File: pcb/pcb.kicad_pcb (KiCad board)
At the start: 2 copper layers, 4 parts, among them U1 MCP2542FDxMF, U2 STM32G0B1KBUx, U3 MCP1792x-3302xCB

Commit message: unrouted nets 0
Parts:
- added C1: 2.2u, Capacitor_SMD:C_0603_1608Metric, F.Cu at (206.8, 53.3)
- added C10: 100n, Capacitor_SMD:C_0402_1005Metric, F.Cu at (185.4, 61.8)
- added C11: 100n, Capacitor_SMD:C_0402_1005Metric, F.Cu at (189.3, 54.7)
- added C12: 100n, Capacitor_SMD:C_0402_1005Metric, F.Cu at (190.6, 53.3)
- added C13: 4.7u, Capacitor_SMD:C_0603_1608Metric, F.Cu at (188.9, 53.3)
- added C2: 2.2u, Capacitor_SMD:C_0603_1608Metric, F.Cu at (212.1, 54.0)
- added C3: 100n, Capacitor_SMD:C_0402_1005Metric, F.Cu at (212.2, 64.8)
- added C4: 1u, Capacitor_SMD:C_0603_1608Metric, F.Cu at (210.8, 64.3)
- added C5: 1u, Capacitor_SMD:C_0402_1005Metric, F.Cu at (206.9, 62.6)
- added C6: 1u, Capacitor_SMD:C_0402_1005Metric, F.Cu at (206.9, 60.5)
- added C7: 100n, Capacitor_SMD:C_0402_1005Metric, F.Cu at (184.7, 53.8)
- added C8: 1u, Capacitor_SMD:C_0603_1608Metric, F.Cu at (186.2, 54.2)
- added C9: 100n, Capacitor_SMD:C_0402_1005Metric, F.Cu at (189.4, 64.1)
- added J1: Conn_01x04_MountingPin, goatworks-footprint-library:CONN04_5055670471_MOL, F.Cu at (215.9, 57.5)
- added J2: Conn_01x04_MountingPin, goatworks-footprint-library:CONN04_5055670471_MOL, F.Cu at (181.2, 60.9)
- added J4: Conn_ARM_SWD_TagConnect_TC2030-NL, Connector:Tag-Connect_TC2030-IDC-NL_2x03_P1.27mm_Vertical, F.Cu at (201.7, 54.2)
- added JP1: SolderJumper_2_Open, Jumper:SolderJumper-2_P1.3mm_Open_RoundedPad1.0x1.5mm, F.Cu at (206.9, 65.1)
- added LS1: Speaker_Crystal, goatworks-footprint-library:PKMCS0909E4000-R1, F.Cu at (201.0, 61.5)
- added M2: ~, goatworks-footprint-library:MP34DT05-A, F.Cu at (214.9, 64.2)
- moved U3 106.3 mm to (209.4, 54.6), turned to -45 degrees
- moved U2 92.8 mm to (192.9, 56.1), turned to -45 degrees
- moved U1 86.9 mm to (186.8, 64.1), turned to 180 degrees
- moved M1 77.2 mm to (182.2, 54.2), turned to 90 degrees
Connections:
- M1 pad 2: unconnected-(M1-LR-Pad2) -> GND
- M1 pad 3: unconnected-(M1-CLK-Pad3) -> /SCL
- M1 pad 4: unconnected-(M1-DOUT-Pad4) -> /SDA
- U1 pad 1: unconnected-(U1-TXD-Pad1) -> /CAN_TX
- U1 pad 2: Net-(U1-VSS-Pad2) -> GND
- U1 pad 3: unconnected-(U1-VDD-Pad3) -> +5V
- U1 pad 4: unconnected-(U1-RXD-Pad4) -> /CAN_RX
- U1 pad 5: unconnected-(U1-VIO-Pad5) -> +3V3
- U1 pad 8: unconnected-(U1-STBY-Pad8) -> /STBY
- U1 pad 9: Net-(U1-VSS-Pad2) -> GND
- U2 pad 11: unconnected-(U2-PA4-Pad11) -> /SPEAKER
- U2 pad 15: unconnected-(U2-PB0-Pad15) -> /CAN_RX
- U2 pad 16: unconnected-(U2-PB1-Pad16) -> /CAN_TX
- U2 pad 24: unconnected-(U2-PA13-Pad24) -> /SWDIO
- U2 pad 25: unconnected-(U2-PA14-Pad25) -> /SWCLK
- U2 pad 27: unconnected-(U2-PB3-Pad27) -> /SCL
- U2 pad 28: unconnected-(U2-PB4-Pad28) -> /SDA
- U2 pad 33: Net-(U2-VSS-Pad33) -> GND
- U2 pad 4: unconnected-(U2-VDD-Pad4) -> +3V3
- U2 pad 5: Net-(U2-VSS-Pad33) -> GND
- U2 pad 6: unconnected-(U2-PF2-Pad6) -> /RESET
- U3 pad 1: unconnected-(U3-GND-Pad1) -> GND
- U3 pad 2: unconnected-(U3-VO-Pad2) -> +3V3
- U3 pad 3: unconnected-(U3-VI-Pad3) -> +5V
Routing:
- net +3V3: track 0.00 -> 77.9 mm, vias 0 -> 4
- net /SCL: track 0.00 -> 57.2 mm, vias 0 -> 3
- net /SDA: track 0.00 -> 49.8 mm, vias 0 -> 3
- net +5V: track 0.00 -> 43.4 mm, vias 0 -> 3
- net /CANL: track 0.00 -> 42.2 mm, vias 0 -> 2
- net /CANH: track 0.00 -> 41.8 mm, vias 0 -> 2
- net /RESET: track 0.00 -> 14.6 mm, vias 0 -> 2
- net /SPEAKER: track 0.00 -> 9.76 mm, vias 0 -> 2
- net /CAN_TX: track 0.00 -> 9.14 mm
- net /CAN_RX: track 0.00 -> 7.95 mm
- net /SWDIO: track 0.00 -> 7.83 mm
- net Net-(JP1-A): track 0.00 -> 6.60 mm
- net /SWCLK: track 0.00 -> 6.53 mm
- net GND: track 0.00 -> 4.26 mm, vias 0 -> 25
- added copper zone on B.Cu, net GND
- added copper zone on F.Cu, net GND
- added copper zone on In1.Cu, net GND
- added copper zone on In2.Cu, net GND
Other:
- board outline added: 40 x 15 mm
- copper layers 2 -> 4

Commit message: drc
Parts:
- moved JP1 0.70 mm to (207.6, 65.1)
- moved LS1 0.30 mm to (201.3, 61.5)
- moved C11 0.10 mm to (189.2, 54.7)
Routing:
- net /SCL: track 57.2 -> 53.4 mm
- net GND: track 4.26 -> 7.14 mm, vias 25 -> 28
- net Net-(JP1-A): track 6.60 -> 7.30 mm
- net /CANL: track 42.2 -> 41.5 mm

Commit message: more vias
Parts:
- moved J4 0.63 mm to (201.5, 54.8)
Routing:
- net +3V3: track 78.1 -> 73.3 mm, vias 4 -> 5
- net GND: track 7.14 -> 7.19 mm, vias 28 -> 35

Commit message: improve routing
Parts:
- removed C5, C6: 1u, Capacitor_SMD:C_0402_1005Metric
- removed JP1: SolderJumper_2_Open, Jumper:SolderJumper-2_P1.3mm_Open_RoundedPad1.0x1.5mm
- added C14: 4.7u, Capacitor_SMD:C_0603_1608Metric, F.Cu at (194.6, 61.6)
- moved C10 0.80 mm to (186.2, 61.8)
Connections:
- LS1 pad 1: Net-(JP1-A) -> GND
- LS1 pad 2: /SPEAKER -> Net-(C14-Pad2)
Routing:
- net +3V3: track 73.3 -> 64.3 mm
- net Net-(JP1-A): track 7.30 -> 0.00 mm
- net /SCL: track 53.4 -> 49.9 mm
- net /SPEAKER: track 9.76 -> 7.52 mm
- net GND: track 7.19 -> 8.87 mm, vias 35 -> 41
- net Net-(C14-Pad2): track 0.00 -> 1.59 mm
- net /SDA: track 49.7 -> 50.9 mm
- net /SWCLK: track 6.58 -> 7.62 mm
- net /RESET: track 15.2 -> 16.0 mm
- net /CANH: track 41.8 -> 42.4 mm
- net +5V: track 43.4 -> 44.0 mm

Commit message: re route!!!
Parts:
- added C15: 100n, Capacitor_SMD:C_0402_1005Metric, F.Cu at (176.3, 52.4)
- added C16: 100n, Capacitor_SMD:C_0402_1005Metric, F.Cu at (226.2, 66.5)
- added D1: CAN_TVS, Package_TO_SOT_SMD:SOT-23-3, F.Cu at (188.0, 64.5)
- added M3: ~, goatworks-footprint-library:T3902, F.Cu at (173.5, 53.1)
- added M4: ~, goatworks-footprint-library:T3902, F.Cu at (223.0, 65.2)
- moved C2 21.1 mm to (191.1, 56.0), turned to 0 degrees
- moved U3 19.0 mm to (190.4, 53.6), turned to 180 degrees
- moved U1 18.8 mm to (205.5, 63.1), turned to -45 degrees
- moved C10 18.3 mm to (204.2, 65.0), turned to 135 degrees
- moved C9 14.5 mm to (203.6, 61.2), turned to 45 degrees
- moved C1 13.7 mm to (193.1, 53.5), turned to -90 degrees
- moved U2 9.91 mm to (202.8, 55.7), turned to 0 degrees
- moved C11 9.63 mm to (198.7, 56.3), turned to 0 degrees
- moved C13 8.86 mm to (197.7, 54.3), turned to 90 degrees
- moved C12 8.54 mm to (199.0, 54.8), turned to 90 degrees
- moved J4 8.06 mm to (209.5, 53.8), turned to 0 degrees
- moved C14 6.72 mm to (201.3, 60.8), turned to -90 degrees
- moved LS1 6.40 mm to (194.9, 61.6), turned to 180 degrees
- moved C4 0.40 mm to (211.2, 64.3)
- moved C3 0.20 mm to (212.4, 64.8)
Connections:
- net /CANH renamed /CAN+
- net /CANL renamed /CAN-
- net /SCL renamed /I2S_CLK
- M1 pad 4: /SDA -> /I2S_SD
- M2 pad 4: /SDA -> /I2S_SD
- U2 pad 28: /SDA -> unconnected-(U2-PB4-Pad28)
- U2 pad 29: unconnected-(U2-PB5-Pad29) -> /I2S_SD
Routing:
- net /SDA: track 50.9 -> 0.00 mm, vias 3 -> 0
- net /I2S_SD: track 0.00 -> 40.8 mm, vias 0 -> 3
- net /CAN-: track 41.1 -> 48.5 mm, vias 2 -> 3
- net /CAN+: track 42.4 -> 48.5 mm, vias 2 -> 3
- net GND: track 8.87 -> 2.89 mm, vias 41 -> 21
- net /I2S_CLK: track 49.9 -> 44.1 mm
- net /CAN_TX: track 9.14 -> 3.40 mm
- net /SPEAKER: track 7.52 -> 2.30 mm, vias 2 -> 0
- net /SWDIO: track 7.98 -> 3.94 mm
- net +3V3: track 64.3 -> 61.1 mm, vias 5 -> 2
- net +5V: track 44.0 -> 46.2 mm
- net /CAN_RX: track 7.72 -> 5.56 mm
- net /SWCLK: track 7.62 -> 5.75 mm
- net /RESET: track 16.0 -> 14.2 mm

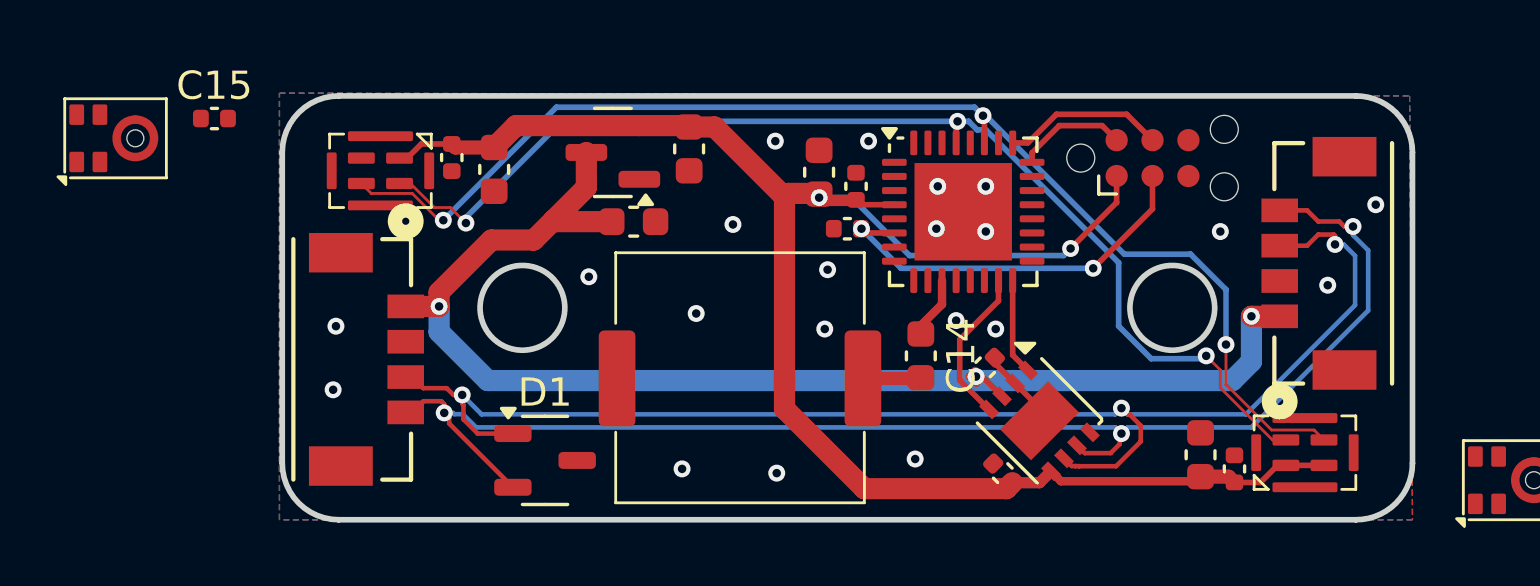
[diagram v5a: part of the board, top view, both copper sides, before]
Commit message: routed with STM mic
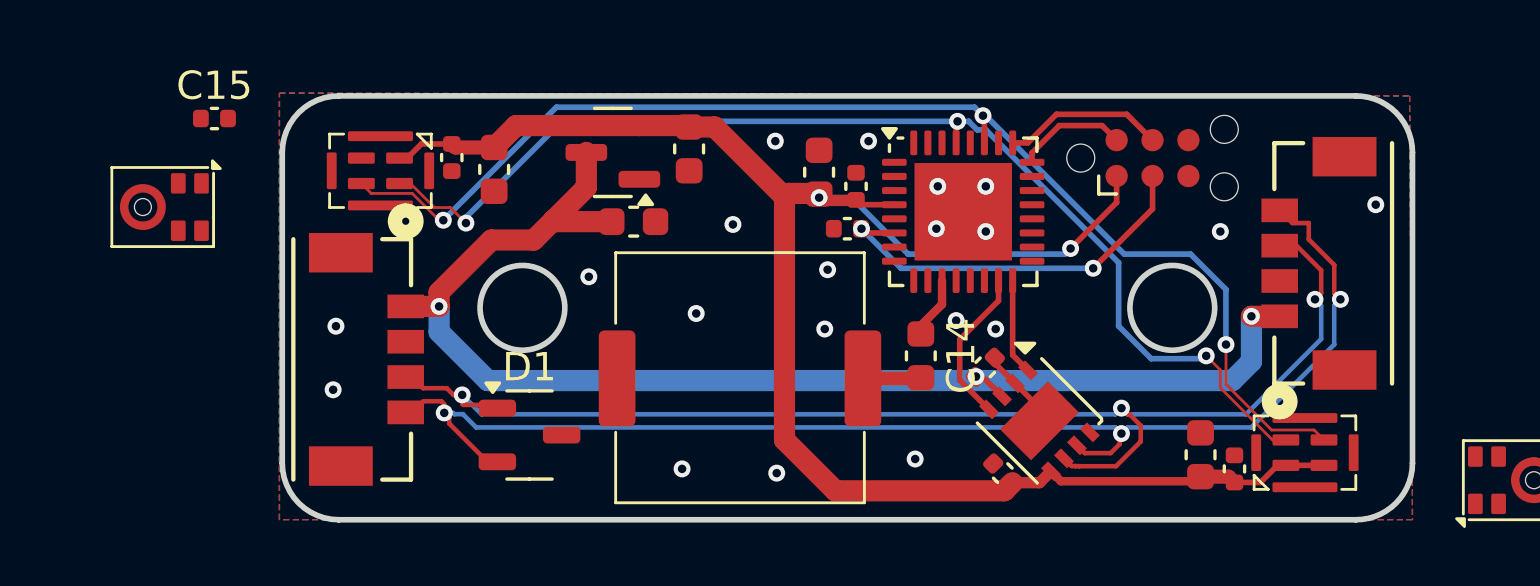
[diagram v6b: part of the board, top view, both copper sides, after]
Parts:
- moved M3 2.45 mm to (173.8, 55.5), turned to 180 degrees
- moved D1 1.05 mm to (187.4, 63.6)
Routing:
- net /CAN-: track 48.5 -> 45.0 mm
- net /CAN+: track 48.5 -> 45.9 mm
- net +3V3: track 61.1 -> 61.7 mm
- net GND: vias 21 -> 20

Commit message: T3902 Mic
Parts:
- removed C3, C7: 100n, Capacitor_SMD:C_0402_1005Metric
- removed C4, C8: 1u, Capacitor_SMD:C_0603_1608Metric
- removed M1, M2: ~, goatworks-footprint-library:MP34DT05-A
- moved C16 12.5 mm to (214.3, 62.7), turned to 180 degrees
- moved M3 8.23 mm to (181.7, 53.5)
- moved M4 7.37 mm to (215.7, 64.7)
- moved C15 7.31 mm to (182.9, 55.5)
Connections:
- U2 pad 19: unconnected-(U2-PA9/UCPD1_DBCC1-Pad19) -> /SWO
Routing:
- net /SWO: track 0.00 -> 7.59 mm
- net +3V3: track 61.7 -> 65.6 mm, vias 2 -> 4
- net /I2S_SD: track 40.8 -> 39.2 mm
- net /I2S_CLK: track 44.1 -> 42.9 mm
- net GND: vias 20 -> 23

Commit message: pcb fixes
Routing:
- net /CAN+: track 45.9 -> 43.7 mm
- net /CAN-: track 45.0 -> 43.6 mm
- net GND: vias 23 -> 39
